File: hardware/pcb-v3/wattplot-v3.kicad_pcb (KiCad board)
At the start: 2 copper layers, 80 x 60 mm, 0 parts

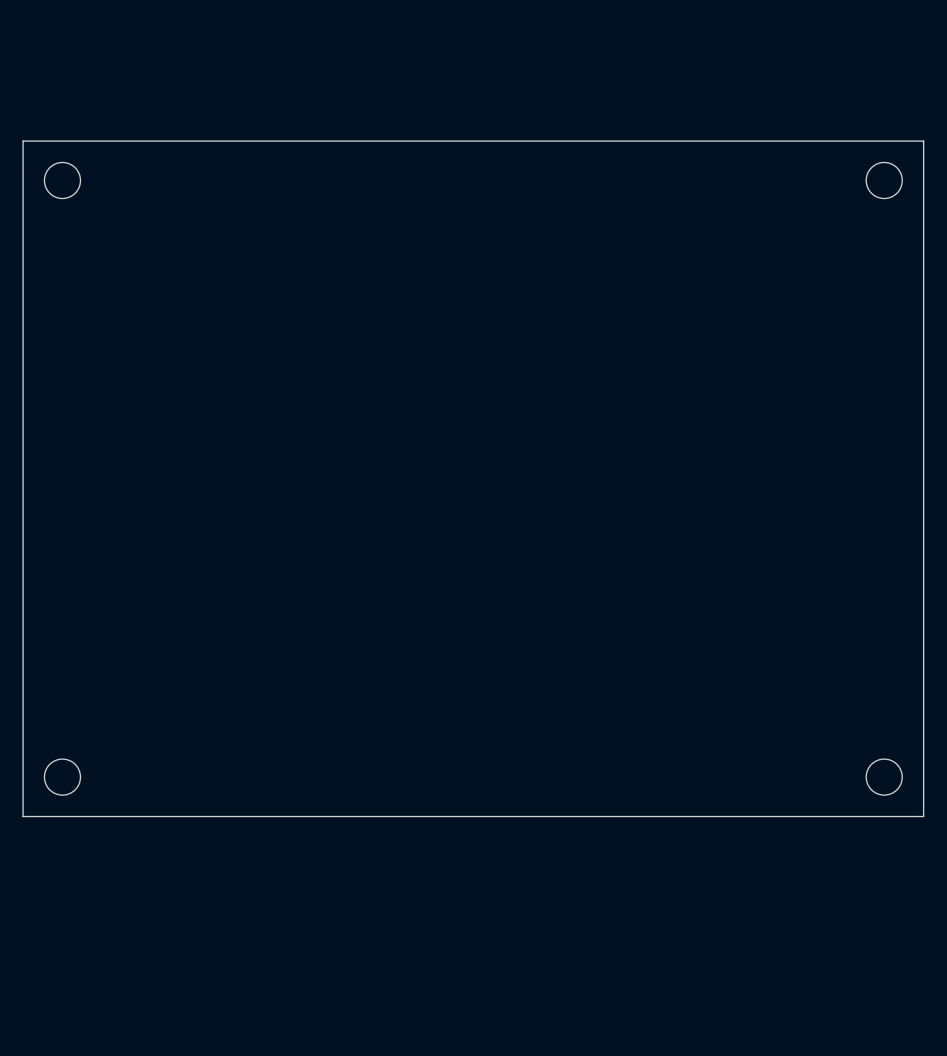
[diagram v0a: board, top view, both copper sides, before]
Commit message: hardware(pcb-v3): add import_schematic.py + 44 footprints seeded
- import_schematic.py: replicates F8 (Update PCB from Schematic)
  * Parses schematic S-expr, extracts each (symbol ...) block
  * Looks up footprint in KiCad's installed libraries
  * Has a LIB_MAP for symbol-lib → footprint-lib name differences
  * Has FOOTPRINT_OVERRIDES for the sch's wrong assignments:
    - U5, U6 (DRV8871) → HTSSOP-28, not HTSOP-8
    - J1 (XT60) → AMASS_XT60, not USB-C
    - SW1, SW2 (tactile) → 6x6, not "SW_Push"
    - J3-J8 (JST) → XH-A series, not PH-K

- place_components.py: corrected refs to match actual sch refs
  * D1 (TVS) not D2
  * R9/R11 not R10
  * TP1, TP3 only (no TP2, TP4, TP5)
  * Added C7, C8, C10, C12, C13, J7, J8
  * Used EDA_ANGLE for SetOrientation (KiCad 10 API)

Result: all 44 components on board, placed by subsystem, no GUI required.
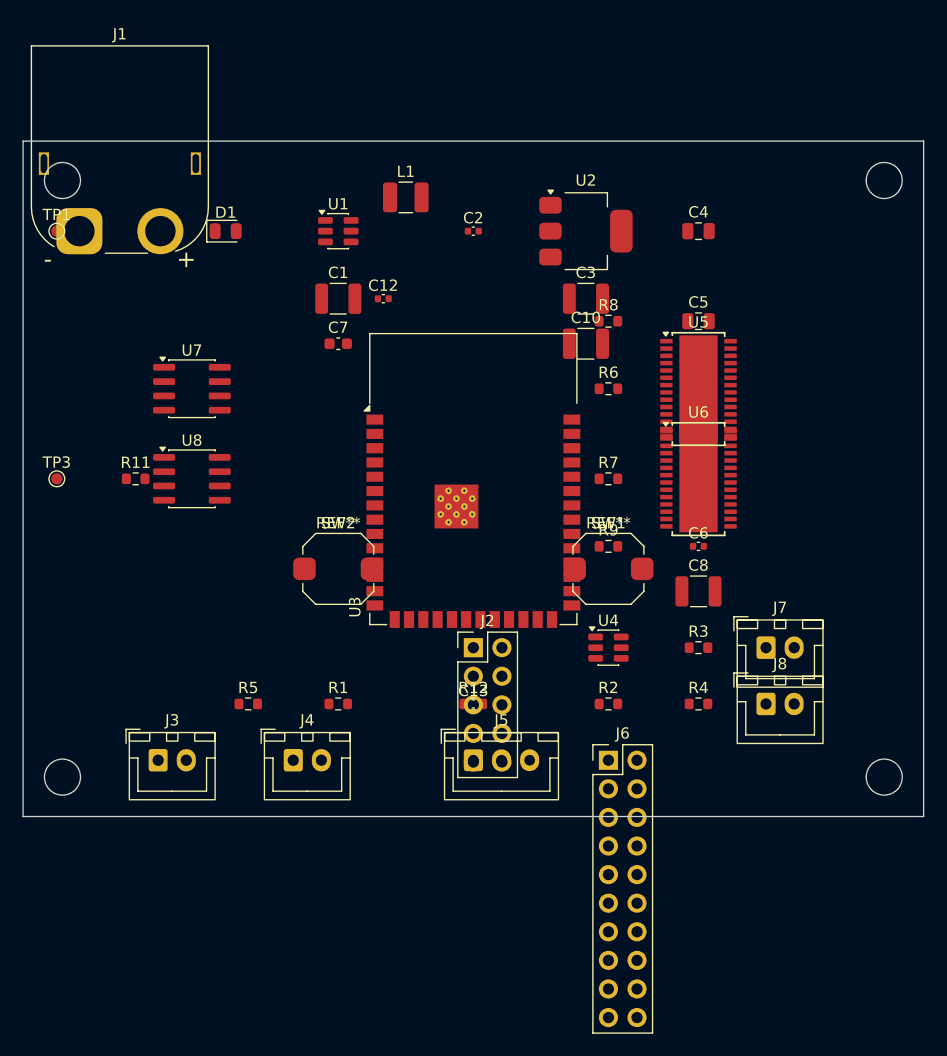
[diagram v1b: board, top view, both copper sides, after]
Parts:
- added C1: 22uF/25V, C_1210_3225Metric, F.Cu at (28.0, 14.0)
- added C10: 22uF/25V, C_1210_3225Metric, F.Cu at (50.0, 18.0)
- added C12: 100nF, C_0402_1005Metric, F.Cu at (32.0, 14.0)
- added C13: 100nF, C_0402_1005Metric, F.Cu at (40.0, 50.0)
- added C2: 100nF, C_0402_1005Metric, F.Cu at (40.0, 8.00)
- added C3: 22uF/10V, C_1210_3225Metric, F.Cu at (50.0, 14.0)
- added C4: 22uF/10V, C_0805_2012Metric, F.Cu at (60.0, 8.00)
- added C5: 22uF/10V, C_0805_2012Metric, F.Cu at (60.0, 16.0)
- added C6: 100nF, C_0402_1005Metric, F.Cu at (60.0, 36.0)
- added C7: 10uF, C_0603_1608Metric, F.Cu at (28.0, 18.0)
- added C8: 22uF/25V, C_1210_3225Metric, F.Cu at (60.0, 40.0)
- added D1: GREEN, LED_0805_2012Metric, F.Cu at (18.0, 8.00)
- added J1: USB-C, AMASS_XT60PW-M_1x02_P7.20mm_Horizontal, F.Cu at (5.00, 8.00)
- added J2: PROG, PinHeader_2x05_P2.54mm_Vertical, F.Cu at (40.0, 45.0)
- added J3: ACTUATOR, JST_XH_B2B-XH-A_1x02_P2.50mm_Vertical, F.Cu at (12.0, 55.0)
- added J4: SOLENOID, JST_XH_B2B-XH-A_1x02_P2.50mm_Vertical, F.Cu at (24.0, 55.0)
- added J5: 1-WIRE, JST_XH_B3B-XH-A_1x03_P2.50mm_Vertical, F.Cu at (40.0, 55.0)
- added J6: EXP1 GPIO+POWER (FUTURE), PinHeader_2x10_P2.54mm_Vertical, F.Cu at (52.0, 55.0)
- added J7: FROST HEATER, JST_XH_B2B-XH-A_1x02_P2.50mm_Vertical, F.Cu at (66.0, 45.0)
- added J8: FROST LIGHT, JST_XH_B2B-XH-A_1x02_P2.50mm_Vertical, F.Cu at (66.0, 50.0)
- added L1: 4.7uH, L_1210_3225Metric, F.Cu at (34.0, 5.00)
- added R1: 33k, R_0603_1608Metric, F.Cu at (28.0, 50.0)
- added R11: 1k, R_0603_1608Metric, F.Cu at (10.0, 30.0)
- added R12: 4.7k, R_0603_1608Metric, F.Cu at (40.0, 50.0)
- added R2: 10k, R_0603_1608Metric, F.Cu at (52.0, 50.0)
- added R3: 100k 1%, R_0603_1608Metric, F.Cu at (60.0, 45.0)
- added R4: 100k 1%, R_0603_1608Metric, F.Cu at (60.0, 50.0)
- added R5: 330R, R_0603_1608Metric, F.Cu at (20.0, 50.0)
- added R6: 10k, R_0603_1608Metric, F.Cu at (52.0, 22.0)
- added R7: 4.7k, R_0603_1608Metric, F.Cu at (52.0, 30.0)
- added R8: 4.7k, R_0603_1608Metric, F.Cu at (52.0, 16.0)
- added R9: 1k, R_0603_1608Metric, F.Cu at (52.0, 36.0)
- added SW1: RESET, SW_Push_1TS009xxxx-xxxx-xxxx_6x6x5mm, F.Cu at (52.0, 38.0)
- added SW2: BOOT, SW_Push_1TS009xxxx-xxxx-xxxx_6x6x5mm, F.Cu at (28.0, 38.0)
- added TP1: nFAULT_ACT, TestPoint_Pad_D1.0mm, F.Cu at (3.00, 8.00)
- added TP3: nFAULT_SOL, TestPoint_Pad_D1.0mm, F.Cu at (3.00, 30.0)
- added U1: MP1584EN, SOT-23-6, F.Cu at (28.0, 8.00)
- added U2: AMS1117-3.3, SOT-223-3_TabPin2, F.Cu at (50.0, 8.00)
- added U3: ESP32-S3-WROOM-1, ESP32-S3-WROOM-1, F.Cu at (40.0, 30.0)
- added U4: USBLC6-2P6, SOT-23-6, F.Cu at (52.0, 45.0)
- added U5: DRV8871 (ACT), HTSSOP-28-1EP_4.4x9.7mm_P0.65mm_EP3.4x9.5mm, F.Cu at (60.0, 22.0)
- added U6: DRV8871 (SOL), HTSSOP-28-1EP_4.4x9.7mm_P0.65mm_EP3.4x9.5mm, F.Cu at (60.0, 30.0)
- added U7: INA219 (PAN), SOIC-8_3.9x4.9mm_P1.27mm, F.Cu at (15.0, 22.0)
- added U8: INA219 (ACT), SOIC-8_3.9x4.9mm_P1.27mm, F.Cu at (15.0, 30.0)
